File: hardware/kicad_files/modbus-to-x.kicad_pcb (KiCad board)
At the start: 4 copper layers, 62 x 55 mm, 65 parts, among them IC1 ESP32-WROOM-32D_M113DH2800PH3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, J1 PWR, J2 UART, J3 Screw_Terminal_3.5mm_2, J4 SSQ-110-X-X-D, SW1 1825910-7, SW2 1825910-7, U1 AMS1117-3.3, U3 MAX3485, U5 AT24CS64-XHM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

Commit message: revised hw
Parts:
- removed J4: SSQ-110-X-X-D, Connector Receptable 2x10 20POS:SAMTEC_SSQ-110-X-X-D
- added SW_TP4: 5029, project_footprints:KEYSTONE_5029, F.Cu at (96.8, 121.2)
- added VCC5_TP5: 5029, project_footprints:KEYSTONE_5029, F.Cu at (104.8, 104.8)
- C10: footprint Capacitor_SMD:C_0402_1005Metric_Pad0.74x0.62mm_HandSolder -> Capacitor_SMD:C_0805_2012Metric_Pad1.18x1.45mm_HandSolder
- C19: footprint project_footprints:C_0402_1005Metric_Pad0.74x0.62mm_HandSolder -> project_footprints:C_0402_1005Metric_Pad0.74x0.62mm_HandSolder_Modified_Silkscreen
- C24: footprint Capacitor_SMD:C_0805_2012Metric_Pad1.18x1.45mm_HandSolder -> Capacitor_SMD:C_1206_3216Metric_Pad1.33x1.80mm_HandSolder
- C25: footprint Capacitor_SMD:C_1206_3216Metric_Pad1.33x1.80mm_HandSolder -> Capacitor_SMD:C_0805_2012Metric_Pad1.18x1.45mm_HandSolder
- moved D2 4.39 mm to (91.0, 125.7), turned to -90 degrees
- moved C10 1.14 mm to (93.5, 118.8)
- moved D6 0.12 mm to (92.8, 82.8), turned to 0 degrees
- moved D4 0.06 mm to (98.5, 82.8)
- moved D5 0.06 mm to (95.6, 82.8)
- turned R4 to 90 degrees
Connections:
- net /STAT_1 renamed /LED_C
- net /STAT_2 renamed /LED_B
- net /STAT_3 renamed /LED_A
- net Net-(D2-K) renamed /SW_NODE
- net Net-(U7-FB) renamed /FB_NODE
- U7 pad V: (no net) -> GND
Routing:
- net /GPIO_35: track 100.1 -> 0.00 mm, vias 1 -> 0
- net /GPIO_34: track 91.0 -> 0.00 mm, vias 1 -> 0
- net /SPI_CS: track 76.9 -> 0.00 mm, vias 1 -> 0
- net /SPI_MISO: track 74.0 -> 0.00 mm, vias 1 -> 0
- net /SPI_CLK: track 73.8 -> 0.00 mm, vias 1 -> 0
- net /EN: track 83.4 -> 13.4 mm, vias 1 -> 0
- net /GPIO27: track 67.6 -> 0.00 mm, vias 1 -> 0
- net /SPI_MOSI: track 63.7 -> 0.00 mm, vias 1 -> 0
- net /GPIO14: track 58.8 -> 0.00 mm, vias 1 -> 0
- net /GPIO12: track 55.5 -> 0.00 mm, vias 1 -> 0
- net VCC5: track 74.4 -> 37.6 mm
- net /SCL_BUS: track 75.3 -> 38.5 mm, vias 3 -> 2
- net /SDA_BUS: track 72.7 -> 43.5 mm, vias 4 -> 3
- net GND: track 118.3 -> 102.0 mm, vias 38 -> 36
- net VDD33: track 78.8 -> 63.7 mm, vias 16 -> 15
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- added copper zone on F.Cu, net GND
- removed copper zone on F.Cu, net /VBUS_12
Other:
- outline, holes or cut-outs redrawn
- board text added: "C"
- board text added: "VCC_TP"

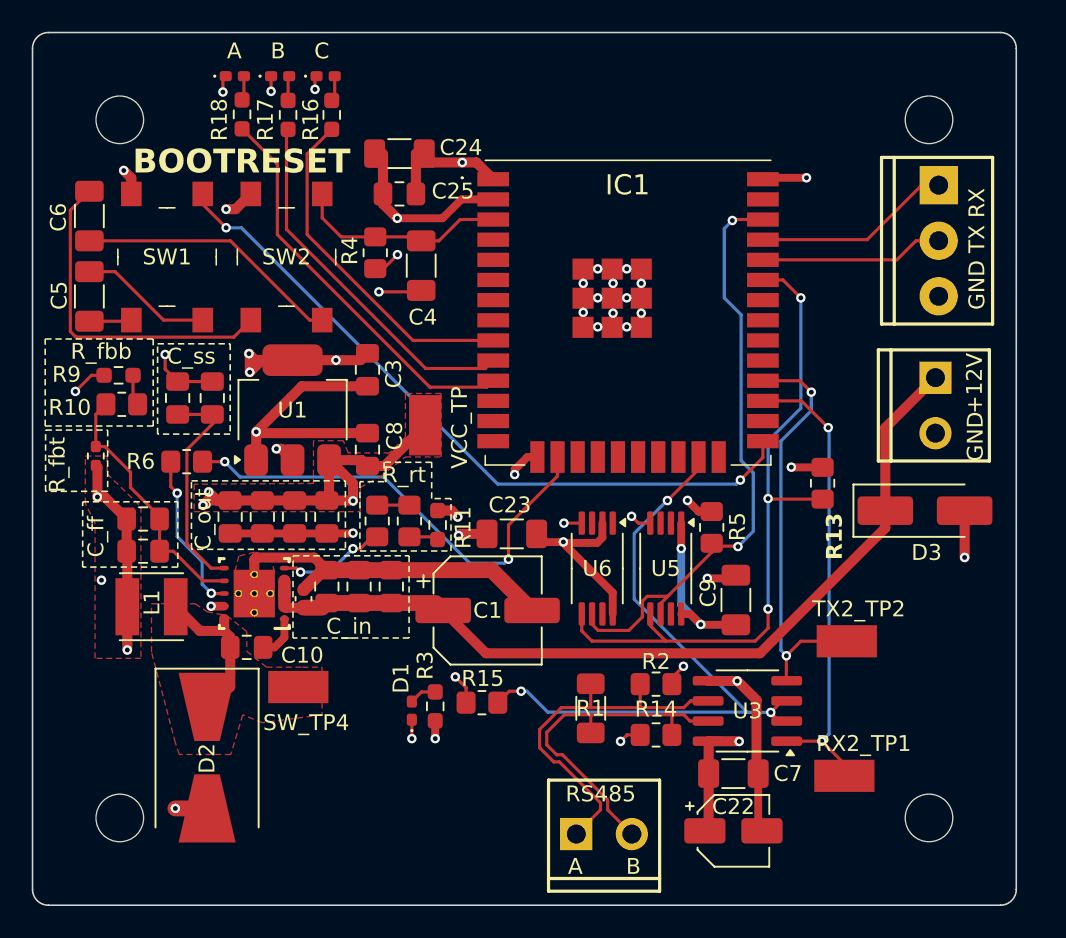
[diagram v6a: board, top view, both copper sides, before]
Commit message: refined MQTT config UI
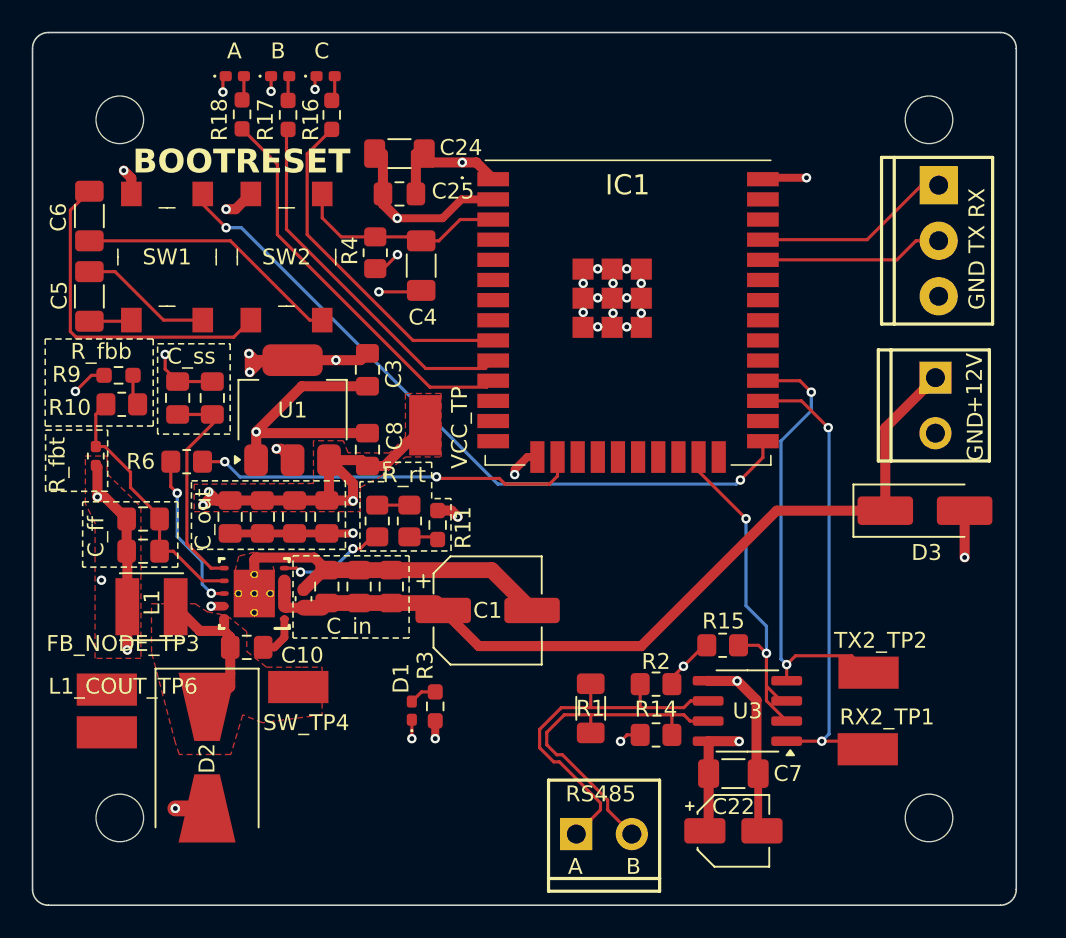
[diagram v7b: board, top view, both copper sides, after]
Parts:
- removed C23, C9: 0.1uF, Capacitor_SMD:C_1206_3216Metric_Pad1.33x1.80mm_HandSolder
- removed R13, R5: 10K, Resistor_SMD:R_0805_2012Metric_Pad1.20x1.40mm_HandSolder
- removed U5, U6: AT24CS64-XHM, Package_SO:TSSOP-8_4.4x3mm_P0.65mm
- added FB_NODE_TP3: 5029, project_footprints:KEYSTONE_5029, F.Cu at (84.7, 121.4)
- added L1_COUT_TP6: 5029, project_footprints:KEYSTONE_5029, F.Cu at (84.7, 124.1)
- moved R15 15.6 mm to (123.5, 118.6)
- moved TX2_TP2 2.41 mm to (132.7, 120.3)
- moved RX2_TP1 2.23 mm to (132.6, 125.2)
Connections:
- U7 pad V: GND -> (no net)
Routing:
- net /SDA_BUS: track 43.5 -> 0.00 mm, vias 3 -> 0
- net /SCL_BUS: track 38.5 -> 0.00 mm, vias 2 -> 0
- net VDD33: track 63.7 -> 38.4 mm, vias 15 -> 9
- net /RS485_DE_RE: track 41.3 -> 22.6 mm, vias 3 -> 2
- net GND: track 102.0 -> 95.8 mm, vias 36 -> 32
- net /PGOOD: track 29.8 -> 24.4 mm
- net /TX_{2}: track 26.7 -> 28.3 mm
- net /VBUS_12: track 54.6 -> 53.6 mm

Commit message: modbus WIP
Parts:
- removed FB_NODE_TP3: 5029, project_footprints:KEYSTONE_5029
- moved L1_COUT_TP6 2.71 mm to (85.3, 121.5)
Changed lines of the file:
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@@
 		(tags "resistor handsolder")
 		(property "Reference" "R15"
-			(at 0.0508 -1.524 360)
+			(at 0.0508 -1.524 0)
 			(layer "F.SilkS")
 			(effects
@@
 		)
 		(property "Value" "10K"
-			(at 0 1.65 360)
+			(at 0 1.65 0)
 			(layer "F.Fab")
 			(effects
@@
 		)
 		(fp_text user "${REFERENCE}"
-			(at 0 0 360)
+			(at 0 0 0)
 			(layer "F.Fab")
 			(effects
@@
 		)
 	)
-	(footprint "project_footprints:KEYSTONE_5029"
-		(layer "F.Cu")
-		(at 84.6836 121.412)
-		(property "Reference" "FB_NODE_TP3"
-			(at 1.02 -2.9 0)
-			(layer "F.SilkS")
-			(effects
-				(font
-					(size 1 1)
-					(thickness 0.15)
-				)
-			)
-		)
-		(property "Value" "5029"
-			(at 6.1 2.9 0)
-			(layer "F.Fab")
-			(effects
-				(font
-					(size 1 1)
-					(thickness 0.15)
-				)
-			)
-		)
-		(property "Footprint" "project_footprints:KEYSTONE_5029"
-			(at 0 0 0)
-			(layer "F.Fab")
-			(hide yes)
-			(effects
-				(font
-					(size 1.27 1.27)
-					(thickness 0.15)
-				)
-			)
-		)
-		(property "Datasheet" "https://www.keyelco.com/product-pdf.cfm?p=1358"
-			(at 0 0 0)
-			(layer "F.Fab")
-			(hide yes)
-			(effects
-				(font
-					(size 1.27 1.27)
-					(thickness 0.15)
-				)
-			)
-		)
-		(property "Description" "PC Test Point, Miniature Phosphor Bronze Silver Plating Surface Mount Mounting Type"
-			(at 0 0 0)
-			(layer "F.Fab")
-			(hide yes)
-			(effects
-				(font
-					(size 1.27 1.27)
-					(thickness 0.15)
-				)
-			)
-		)
-		(sheetname "Root")
-		(sheetfile "modbus-to-x.kicad_sch")
-		(attr smd)
-		(fp_line
-			(start -2.155 -1.265)
-			(end -2.155 1.265)
-			(stroke
-				(width 0.05)
-				(type solid)
-			)
-			(layer "F.CrtYd")
-		)
-		(fp_line
-			(start -2.155 1.265)
-			(end 2.155 1.265)
-			(stroke
-				(width 0.05)
-				(type solid)
-			)
-			(layer "F.CrtYd")
-		)
-		(fp_line
-			(start 2.155 -1.265)
-			(end -2.155 -1.265)
-			(stroke
-				(width 0.05)
-				(type solid)
-			)
-			(layer "F.CrtYd")
-		)
-		(fp_line
-			(start 2.155 1.265)
-			(end 2.155 -1.265)
-			(stroke
-				(width 0.05)
-				(type solid)
-			)
-			(layer "F.CrtYd")
-		)
-		(fp_line
-			(start -1.905 -1.015)
-			(end -1.905 1.015)
-			(stroke
-				(width 0.127)
-				(type solid)
-			)
-			(layer "F.Fab")
-		)
-		(fp_line
-			(start -1.905 1.015)
-			(end 1.905 1.015)
-			(stroke
-				(width 0.127)
-				(type solid)
-			)
-			(layer "F.Fab")
-		)
-		(fp_line
-			(start 1.905 -1.015)
-			(end -1.905 -1.015)
-			(stroke
-				(width 0.127)
-				(type solid)
-			)
-			(layer "F.Fab")
-		)
-		(fp_line
-			(start 1.905 1.015)
-			(end 1.905 -1.015)
-			(stroke
-				(width 0.127)
-				(type solid)
-			)
-			(layer "F.Fab")
-		)
-		(pad "TP" smd rect
-			(at 0 0)
-			(size 3.8 2.03)
-			(layers "F.Cu" "F.Paste" "F.Mask")
-			(net 35 "/FB_NODE")
-			(pintype "passive")
-			(solder_mask_margin 0.102)
-		)
-	)
 	(footprint "LED_SMD:LED_0402_1005Metric_Pad0.77x0.64mm_HandSolder"
 		(layer "F.Cu")
@@
 	(footprint "project_footprints:KEYSTONE_5029"
 		(layer "F.Cu")
-		(at 84.6836 124.1044)
+		(at 85.2932 121.4628)
 		(property "Reference" "L1_COUT_TP6"
 			(at 1.02 -2.9 0)
@@
 	)
 	(segment
-		(start 88.0067 110.5054)
-		(end 86.174 108.6727)
+		(start 84.62415 103.43325)
+		(end 83.9896 104.0678)
 		(width 0.2)
 		(layer "F.Cu")
@@
 	)
 	(segment
-		(start 84.62415 103.43325)
-		(end 83.9896 104.0678)
+		(start 83.9896 104.0678)
+		(end 83.9896 106.094)
 		(width 0.2)
 		(layer "F.Cu")
@@
 	)
 	(segment
-		(start 86.174 107.7075)
-		(end 84.5605 106.094)
+		(start 86.174 107.764)
+		(end 84.504 106.094)
 		(width 0.2)
 		(layer "F.Cu")
@@
 	)
 	(segment
-		(start 83.9896 104.0678)
-		(end 83.9896 106.094)
+		(start 88.0067 110.5054)
+		(end 86.174 108.6727)
 		(width 0.2)
 		(layer "F.Cu")
@@
 	(segment
 		(start 88.0067 110.6581)
-		(end 88.0067 110.607)
+		(end 88.0067 110.5054)
 		(width 0.2)
 		(layer "F.Cu")
@@
 	)
 	(segment
-		(start 86.174 108.6727)
-		(end 86.174 107.7075)
+		(start 88.0067 110.6581)
+		(end 88.0067 110.607)
 		(width 0.2)
 		(layer "F.Cu")
@@
 	)
 	(segment
-		(start 88.0067 110.6581)
-		(end 88.0067 110.5054)
+		(start 86.174 108.6727)
+		(end 86.174 107.764)
 		(width 0.2)
 		(layer "F.Cu")
@@
 	)
 	(segment
-		(start 84.5605 106.094)
-		(end 83.9896 106.094)
+		(start 90.734688 114.557099)
+		(end 88.867689 112.6901)
 		(width 0.2)
 		(layer "F.Cu")
@@
 	)
 	(segment
-		(start 90.734688 114.557099)
-		(end 88.867689 112.6901)
+		(start 84.504 106.094)
+		(end 83.9896 106.094)
 		(width 0.2)
 		(layer "F.Cu")
